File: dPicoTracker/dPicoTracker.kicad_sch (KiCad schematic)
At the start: 9 parts, among them P1 USB_C_Plug_USB2.0, U1 RP2040, U2 LT1963AxST-3.3

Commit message: I think halfway there
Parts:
- removed U2: LT1963AxST-3.3, Package_TO_SOT_SMD:SOT-223-3_TabPin2, symbol Regulator_Linear:LT1963AxST-3.3
- added C5: 10µF, symbol Device:C
- added C6: 15pF, symbol Device:C
- added C7: 1nF, symbol Device:C
- added J1: Conn_01x02_Pin, Connector_PinHeader_2.00mm:PinHeader_1x02_P2.00mm_Vertical, symbol Connector:Conn_01x02_Pin
- added L1: 4.7µH, Inductor_SMD:L_1210_3225Metric, symbol Device:L
- added R3, R4: 1kΩ, symbol Device:R
- added R5: 200kΩ, symbol Device:R
- added R6: 100kΩ, symbol Device:R
- added U2: NCP1117-3.3_SOT223, Package_TO_SOT_SMD:SOT-223-3_TabPin2, symbol Regulator_Linear:NCP1117-3.3_SOT223
- added U3, U4: CJ431, PCM_JLCPCB:SOT-23-3_L2.9-W1.6-P1.90-LS2.8-BR, symbol PCM_JLCPCB-Power:Ref, 2-36V, 100mA, CJ431
- added U5: TPS61221DCK, Package_TO_SOT_SMD:SOT-23-5, symbol Regulator_Switching:TPS61221DCK
- added U6: W25Q128JVS, Package_SO:SOIC-8_5.3x5.3mm_P1.27mm, symbol Memory_Flash:W25Q128JVS
- added X1: ABM8-272-T3, ABM8-272-T3_ABR, symbol 2025-03-29_06-13-32:ABM8-272-T3
- C1: value 22µF -> 100nF
- C2: value 22µF -> 15pF
- C3, C4: value 100nF -> 10µF
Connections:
- net +3V3: now also C1.1, U2.2 (VO), U5.2 (FB), U5.4 (VOUT), U6.8 (VCC); no longer C2.1
- net GND: now also C2.1, C5.2, C6.2, C7.1, J1.1 (Pin_1), R6.2, U2.1 (GND), U4.3 (AN), U5.3 (GND), U6.4 (GND), X1.2, X1.4; no longer C2.2
- net VBUS: now also C5.1, L1.1, R5.1, U2.3 (VI), U5.1 (VIN), U5.6 (EN); no longer C1.1
- new net: L1.2, U5.5 (L)
- new net: J1.2 (Pin_2), R3.1
- new net: U3.3 (AN), U4.1 (REF), U4.2 (CAT)
- new net: C6.1, R4.1, X1.3
- new net MEASURE_VBAT: C7.2, R5.2, R6.1
- new net QSPI_CLK: U6.6 (CLK)
- new net QSPI_SD0: U6.5 (DI/IO_{0})
- new net QSPI_SD1: U6.2 (DO/IO_{1})
- new net QSPI_SD2: U6.3 (~{WP}/IO_{2})
- new net QSPI_SD3: U6.7 (~{HOLD}/~{RESET}/IO_{3})
- new net QSPI_SS: R3.2, U6.1 (~{CS})
- new net VCC: U3.1 (REF), U3.2 (CAT)
- new net XIN: C2.2, X1.1
- new net XOUT: R4.2
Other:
- note added: "Battery measurement vdiv"
- note added: "Buck-Boost converter"
- note added: "Flash"
- note added: "Oscillator"
- note added: "Shunt"
- moved on the sheet: U1

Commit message: add schematic
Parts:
- C1, C2, C3, C4, C5, C6, C7: footprint (none) -> PCM_JLCPCB:C_1206
- L1: footprint Inductor_SMD:L_1210_3225Metric -> PCM_JLCPCB:L_1206
- P1: footprint (none) -> Connector_USB:USB_C_Receptacle_XKB_U262-16XN-4BVC11
- R1, R2, R3, R4, R5, R6: footprint (none) -> PCM_JLCPCB:R_1206
- X1: footprint ABM8-272-T3_ABR -> footprints:ABM8-272-T3_ABR
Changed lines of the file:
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@@
 			)
 		)
-		(property "Footprint" ""
+		(property "Footprint" "PCM_JLCPCB:C_1206"
 			(at 36.5252 33.02 0)
 			(effects
@@
 			)
 		)
-		(property "Footprint" ""
+		(property "Footprint" "PCM_JLCPCB:C_1206"
 			(at 81.5848 121.92 0)
 			(effects
@@
 			)
 		)
-		(property "Footprint" ""
+		(property "Footprint" "Connector_USB:USB_C_Receptacle_XKB_U262-16XN-4BVC11"
 			(at 29.21 72.39 0)
 			(effects
@@
 			)
 		)
-		(property "Footprint" "Inductor_SMD:L_1210_3225Metric"
+		(property "Footprint" "PCM_JLCPCB:L_1206"
 			(at 31.75 114.3 0)
 			(effects
@@
 			)
 		)
-		(property "Footprint" ""
+		(property "Footprint" "PCM_JLCPCB:C_1206"
 			(at 147.0152 34.29 0)
 			(effects
@@
 			)
 		)
-		(property "Footprint" ""
+		(property "Footprint" "PCM_JLCPCB:R_1206"
 			(at 116.84 46.228 90)
 			(effects
@@
 			)
 		)
-		(property "Footprint" ""
+		(property "Footprint" "PCM_JLCPCB:C_1206"
 			(at 16.8148 151.13 0)
 			(effects
@@
 			)
 		)
-		(property "Footprint" "ABM8-272-T3_ABR"
+		(property "Footprint" "footprints:ABM8-272-T3_ABR"
 			(at 27.94 151.13 0)
 			(effects
@@
 			)
 		)
-		(property "Footprint" ""
+		(property "Footprint" "PCM_JLCPCB:R_1206"
 			(at 49.022 66.04 90)
 			(effects
@@
 			)
 		)
-		(property "Footprint" ""
+		(property "Footprint" "PCM_JLCPCB:R_1206"
 			(at 92.202 111.76 90)
 			(effects
@@
 			)
 		)
-		(property "Footprint" ""
+		(property "Footprint" "PCM_JLCPCB:R_1206"
 			(at 92.202 125.73 90)
 			(effects
@@
 			)
 		)
-		(property "Footprint" ""
+		(property "Footprint" "PCM_JLCPCB:R_1206"
 			(at 51.562 170.18 90)
 			(effects
@@
 			)
 		)
-		(property "Footprint" ""
+		(property "Footprint" "PCM_JLCPCB:R_1206"
 			(at 60.452 66.04 90)
 			(effects
@@
 			)
 		)
-		(property "Footprint" ""
+		(property "Footprint" "PCM_JLCPCB:C_1206"
 			(at 28.9052 125.73 0)
 			(effects
@@
 			)
 		)
-		(property "Footprint" ""
+		(property "Footprint" "PCM_JLCPCB:C_1206"
 			(at 68.2752 33.02 0)
 			(effects
@@
 			)
 		)
-		(property "Footprint" ""
+		(property "Footprint" "PCM_JLCPCB:C_1206"
 			(at 60.96 160.3248 0)
 			(effects

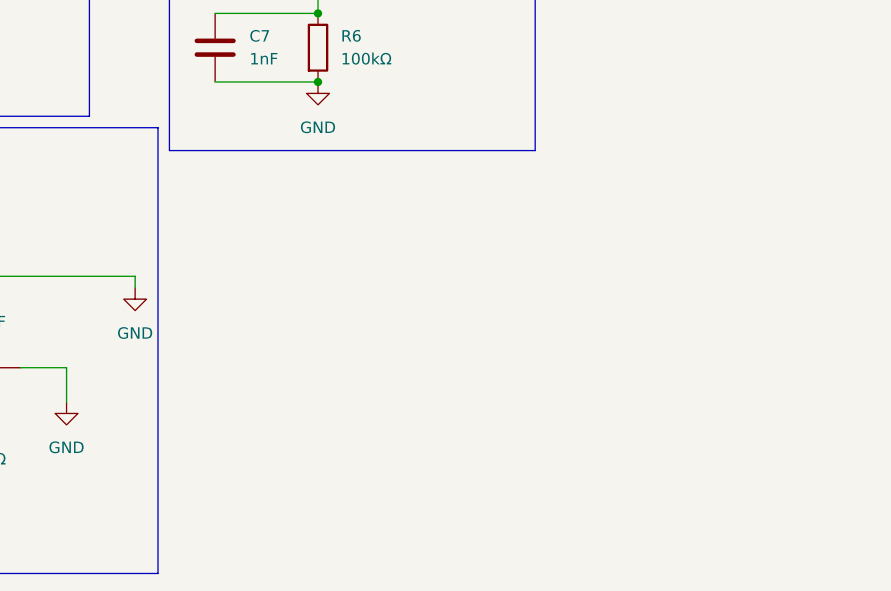
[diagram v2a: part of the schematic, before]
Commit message: Add power supervisor
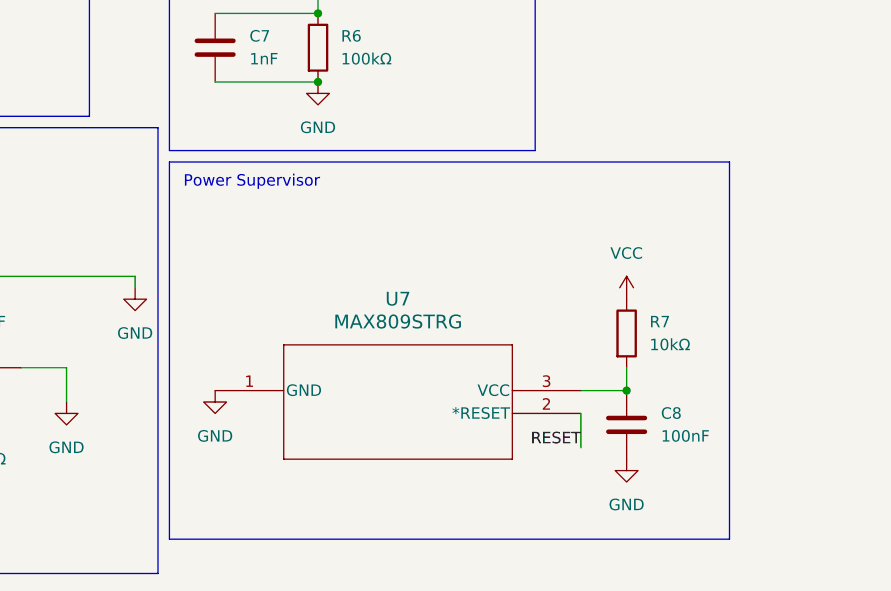
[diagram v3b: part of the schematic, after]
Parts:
- added C8: 100nF, PCM_JLCPCB:C_1206, symbol Device:C
- added R7: 10kΩ, PCM_JLCPCB:R_1206, symbol Device:R
- added U7: MAX809STRG, footprints1:SOT-23_ONS, symbol 2025-05-11_20-58-27:MAX809STRG
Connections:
- net GND: now also C8.2, U7.1 (GND)
- net VCC: now also R7.1
- new net: C8.1, R7.2, U7.3 (VCC)
- new net RESET: U7.2 (*RESET)
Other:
- note added: "Power Supervisor"

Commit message: add VFO
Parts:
- added C10, C9: 100nF, symbol Device:C
- added Q1: AO3401A, PCM_JLCPCB:Q_SOT-23, symbol PCM_JLCPCB-Transistors:PMOS,AO3401A
- added R8: 10kΩ, symbol Device:R
- added Y1: Si5351A-B-GT, Package_SO:MSOP-10_3x3mm_P0.5mm, symbol Oscillator:Si5351A-B-GT
- added Y2: XOS25026000LT00351005, Crystal:Crystal_SMD_2520-4Pin_2.5x2.0mm, symbol Device:Crystal_GND23
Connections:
- net +3V3: now also Q1.2 (S), R8.1
- net GND: now also C10.2, C9.2, Y1.8 (GND), Y2.1, Y2.2
- new net: C10.1, C9.1, Q1.3 (D), Y1.1 (VDD), Y1.7 (VDDO), Y2.4
- new net VFO_CLK0: Y1.10 (CLK0)
- new net VFO_CLK1: Y1.9 (CLK1)
- new net VFO_CLK2: Y1.6 (CLK2)
- new net VFO_OSC: Y1.2 (XA), Y2.3
- new net VFO_PWR_T: Q1.1 (G), R8.2
- new net VFO_SCL: Y1.4 (SCL)
- new net VFO_SDA: Y1.5 (SDA)
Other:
- note added: "Crystal, 26MHz P1: Tri-state P2: GND P3: OUT P4: VDD"
- note added: "VFO"
- moved on the sheet: U1

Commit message: Add everything except pico + headers
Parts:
- removed U1: RP2040, Package_DFN_QFN:QFN-56-1EP_7x7mm_P0.4mm_EP3.2x3.2mm, symbol MCU_RaspberryPi:RP2040
- added AE1: HF 14MHz ANT, symbol Device:Antenna_Shield
- added AE2: VHF 144MHz ANT, symbol Device:Antenna_Shield
- added C11, C12, C13, C14, C15, C16: C, symbol Device:C
- added C17, C18: 100nF, symbol Device:C
- added D1: LED, symbol Device:LED
- added L2, L3, L4, L5: L, symbol Device:L
- added R10, R9: 2kΩ, symbol Device:R
- added R11, R12, R14, R15: 10kΩ, symbol Device:R
- added R13: R, symbol Device:R
- added U8: BMP280, Package_LGA:Bosch_LGA-8_2x2.5mm_P0.65mm_ClockwisePinNumbering, symbol Sensor_Pressure:BMP280
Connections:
- net +3V3: now also C17.1, C18.1, R14.1, R15.1, U8.2 (CSB), U8.6 (VDDIO), U8.8 (VDD)
- net GND: now also AE1.2 (Shield), AE2.2 (Shield), C11.2, C12.2, C13.2, C14.2, C15.2, C16.2, C17.2, C18.2, D1.1 (K), R10.2, R9.2, U8.1 (GND), U8.5 (SDO), U8.7 (GND)
- net VFO_CLK0: now also C11.1, L2.1
- net VFO_CLK1: now also C14.1, L4.1
- net VFO_SCL: now also R12.2
- net VFO_SDA: now also R11.2
- net VFO_3v3: now reaches C10.1, C9.1, Q1.3 (D), Y1.1 (VDD), Y1.7 (VDDO), Y2.4
- net VFO_3v3: now also R11.1, R12.1
- new net: AE1.1 (A), C12.1, C13.1, L2.2, L3.1, L3.2, R9.1
- new net: AE2.1 (A), C15.1, C16.1, L4.2, L5.1, L5.2, R10.1
- new net: D1.2 (A), R13.2
- new net LED: R13.1
- new net SENS_SCL: R14.2, U8.4 (SCK)
- new net SENS_SDA: R15.2, U8.3 (SDI)
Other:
- added sheet Pico Pinout (untitled.kicad_sch)
- note added: "Filter+Antenna"
- note added: "Temp/Baro"
- moved on the sheet: C1, C2, C6, C7, C8, J1, R3, R4, R5, R6, R7, U3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

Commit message: add all but pico
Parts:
- removed R10: 2kΩ, symbol Device:R
- added AE3: GPS_ANT, symbol Device:Antenna_Shield
- added C19: 100nF, symbol Device:C
- added IC1: ATGM336H-5N31, ATGM336H5N31, symbol ATGM336H-5N31:ATGM336H-5N31
- added Q2: AO3401A, PCM_JLCPCB:Q_SOT-23, symbol PCM_JLCPCB-Transistors:PMOS,AO3401A
- C11, C13: value C -> 240pF
- C12: value C -> 430pF
- C14, C16: value C -> 24pF
- C15: value C -> 43pF
- L2, L3: value L -> 750nH
- L4, L5: value L -> 75nH
- R9: value 2kΩ -> 10kΩ
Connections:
- net +3V3: now also R9.1, IC1.6 (VBAT), Q2.2 (S)
- net GND: now also AE3.2 (Shield), C19.2, IC1.1 (GND_1), IC1.10 (GND_2), IC1.12 (GND_3); no longer R9.2
- net at C15.1, L4.2, L5.1: no longer AE2.1 (A), C16.1, L5.2
- new net: AE1.1 (A), C13.1, L3.2
- new net: C12.1, L2.2, L3.1
- new net: AE3.1 (A), IC1.11 (RF_IN)
- new net: C19.1, IC1.8 (VCC), Q2.3 (D)
- new net: AE2.1 (A), C16.1, L5.2
- new net GPS_1PPS: IC1.4 (1PPS)
- new net GPS_ON: IC1.5 (ON/OFF)
- new net GPS_PWR_T: Q2.1 (G), R9.2
- new net GPS_RESET: IC1.9 (NRESET)
- new net UART1_RX: IC1.2 (TXD)
- new net UART1_TX: IC1.3 (RXD)
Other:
- removed sheet Pico Pinout
- note added: "GPS"
- moved on the sheet: C11, C13, C14

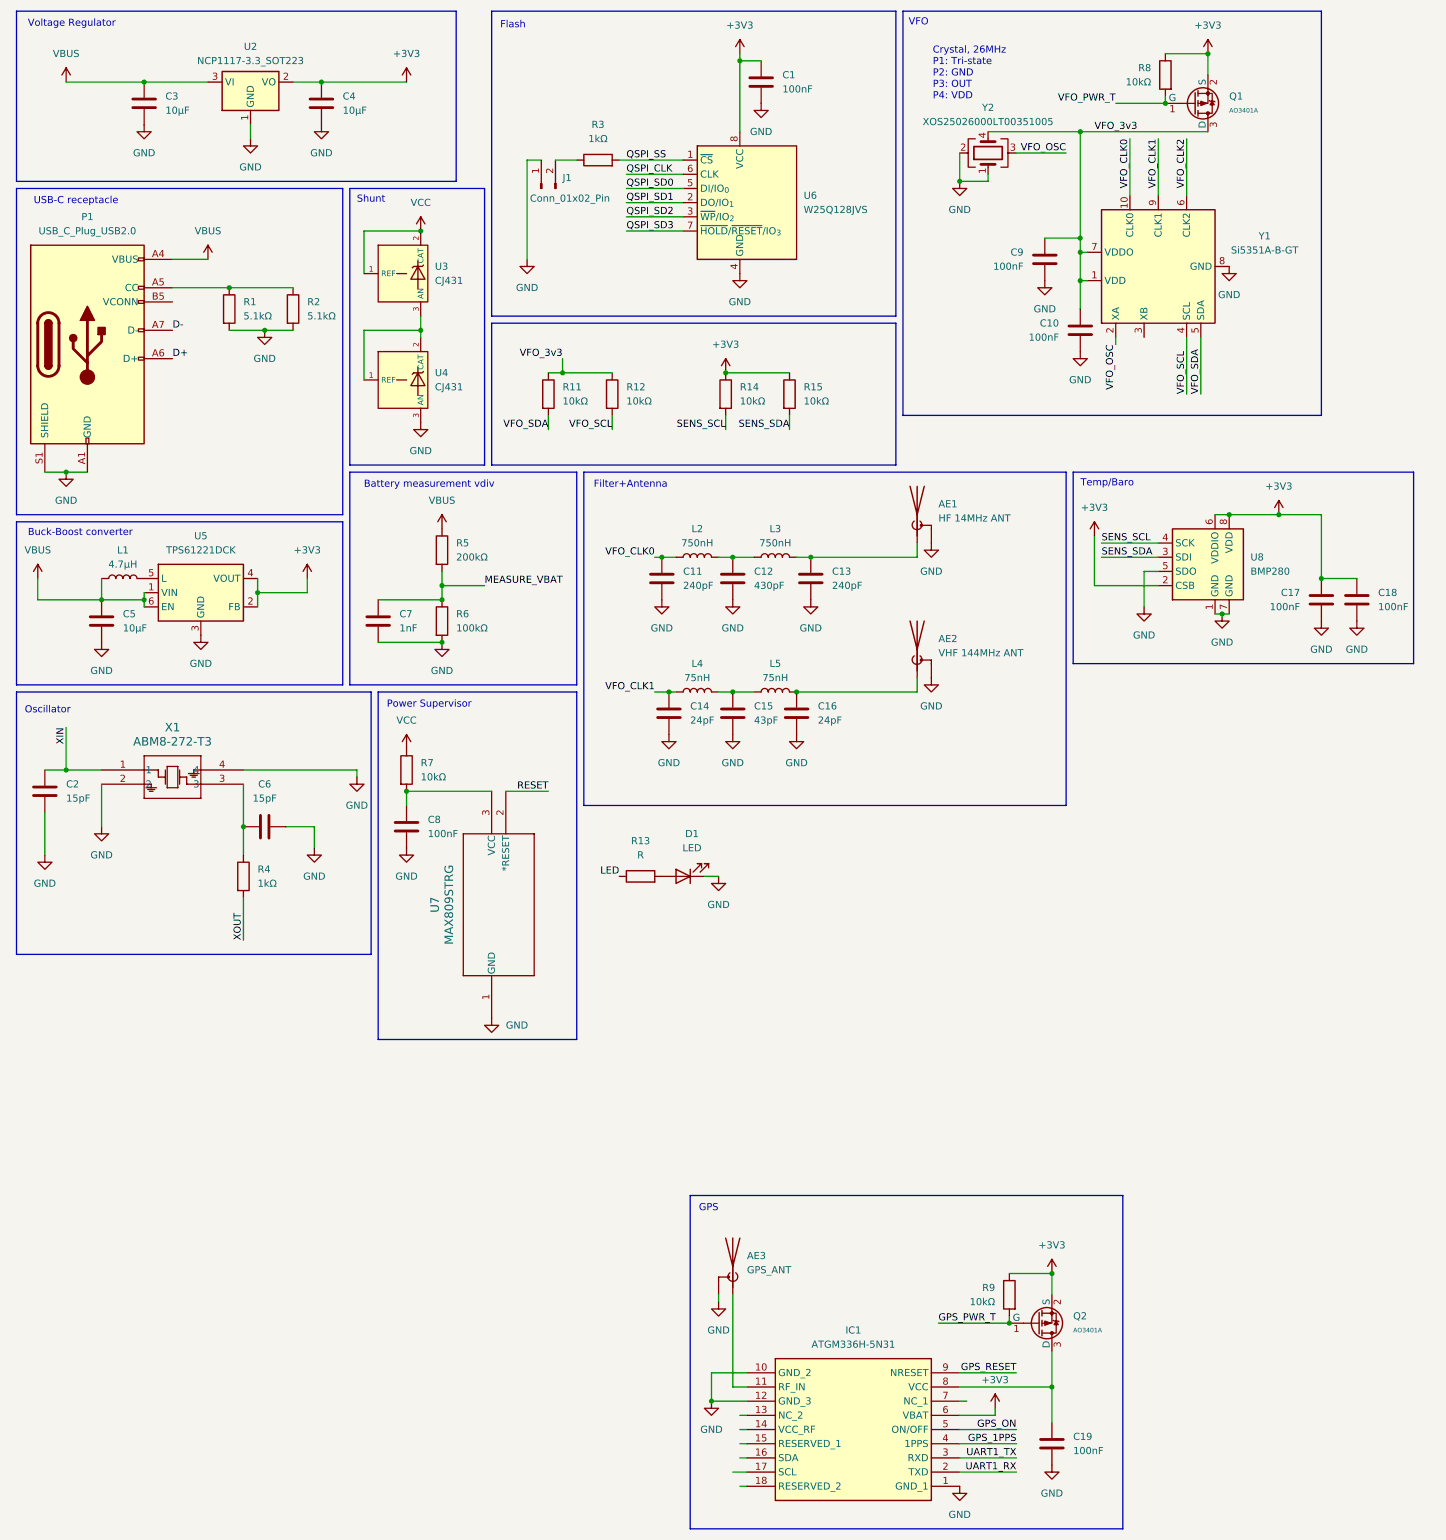
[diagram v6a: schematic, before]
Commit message: swap to pico
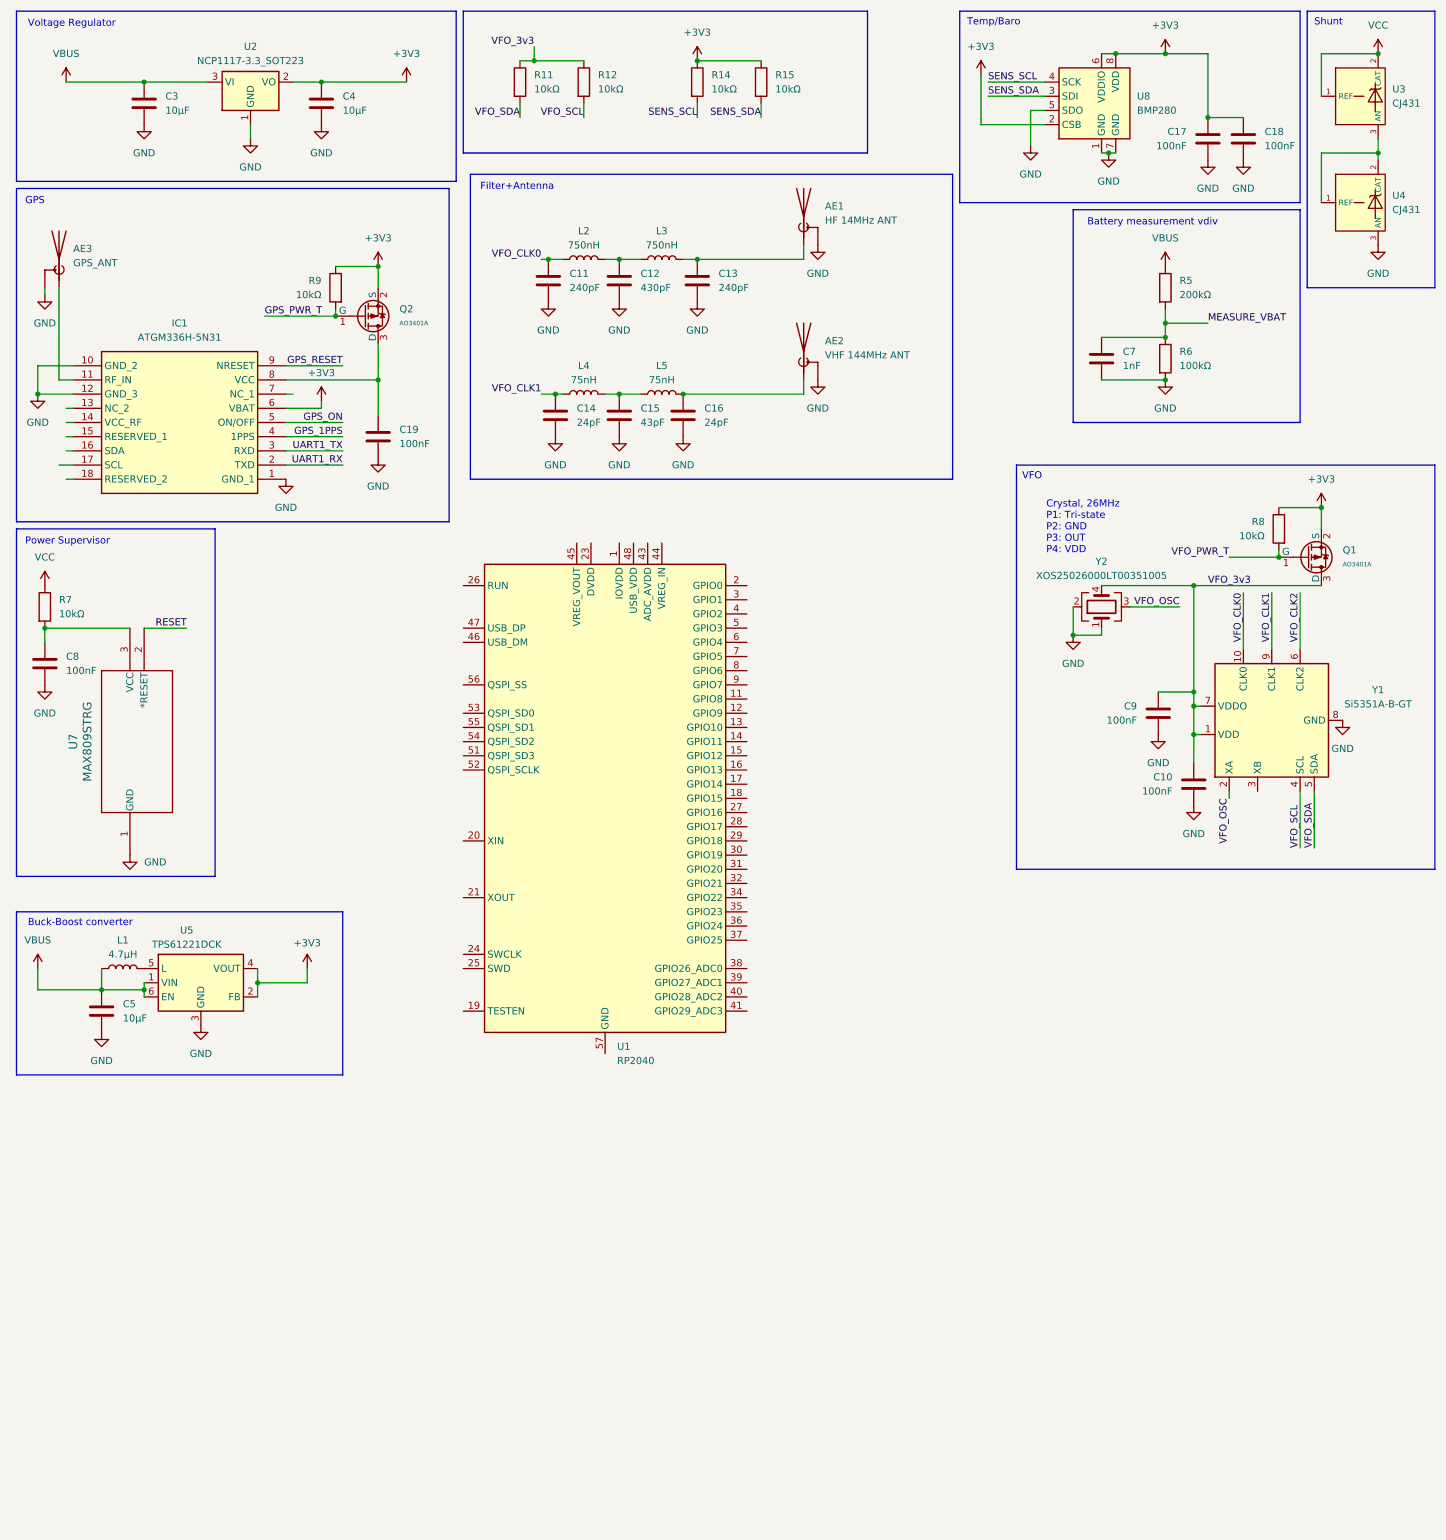
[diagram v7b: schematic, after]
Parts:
- removed C1: 100nF, PCM_JLCPCB:C_1206, symbol Device:C
- removed C2, C6: 15pF, PCM_JLCPCB:C_1206, symbol Device:C
- removed D1: LED, symbol Device:LED
- removed J1: Conn_01x02_Pin, Connector_PinHeader_2.00mm:PinHeader_1x02_P2.00mm_Vertical, symbol Connector:Conn_01x02_Pin
- removed P1: USB_C_Plug_USB2.0, Connector_USB:USB_C_Receptacle_XKB_U262-16XN-4BVC11, symbol Connector:USB_C_Plug_USB2.0
- removed R1, R2: 5.1kΩ, PCM_JLCPCB:R_1206, symbol Device:R
- removed R13: R, symbol Device:R
- removed R3, R4: 1kΩ, PCM_JLCPCB:R_1206, symbol Device:R
- removed U6: W25Q128JVS, Package_SO:SOIC-8_5.3x5.3mm_P1.27mm, symbol Memory_Flash:W25Q128JVS
- removed X1: ABM8-272-T3, footprints:ABM8-272-T3_ABR, symbol 2025-03-29_06-13-32:ABM8-272-T3
- added U1: RP2040, Package_DFN_QFN:QFN-56-1EP_7x7mm_P0.4mm_EP3.2x3.2mm, symbol MCU_RaspberryPi:RP2040
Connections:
- new net: U1.1 (IOVDD), U1.10 (IOVDD), U1.22 (IOVDD), U1.33 (IOVDD), U1.42 (IOVDD), U1.49 (IOVDD)
- new net: U1.23 (DVDD), U1.50 (DVDD)
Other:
- note removed: "Flash"
- note removed: "Oscillator"
- note removed: "USB-C receptacle"
- moved on the sheet: AE1, AE2, AE3, C10, C11, C12, C13, C14, C15, C16, C17, C18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
